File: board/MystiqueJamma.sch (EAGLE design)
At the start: 36 parts, among them IC1 7805, IC2 74LS245N, IC3 74LS245N, IC4 74LS245N, U1 AS6C4008-55PCN

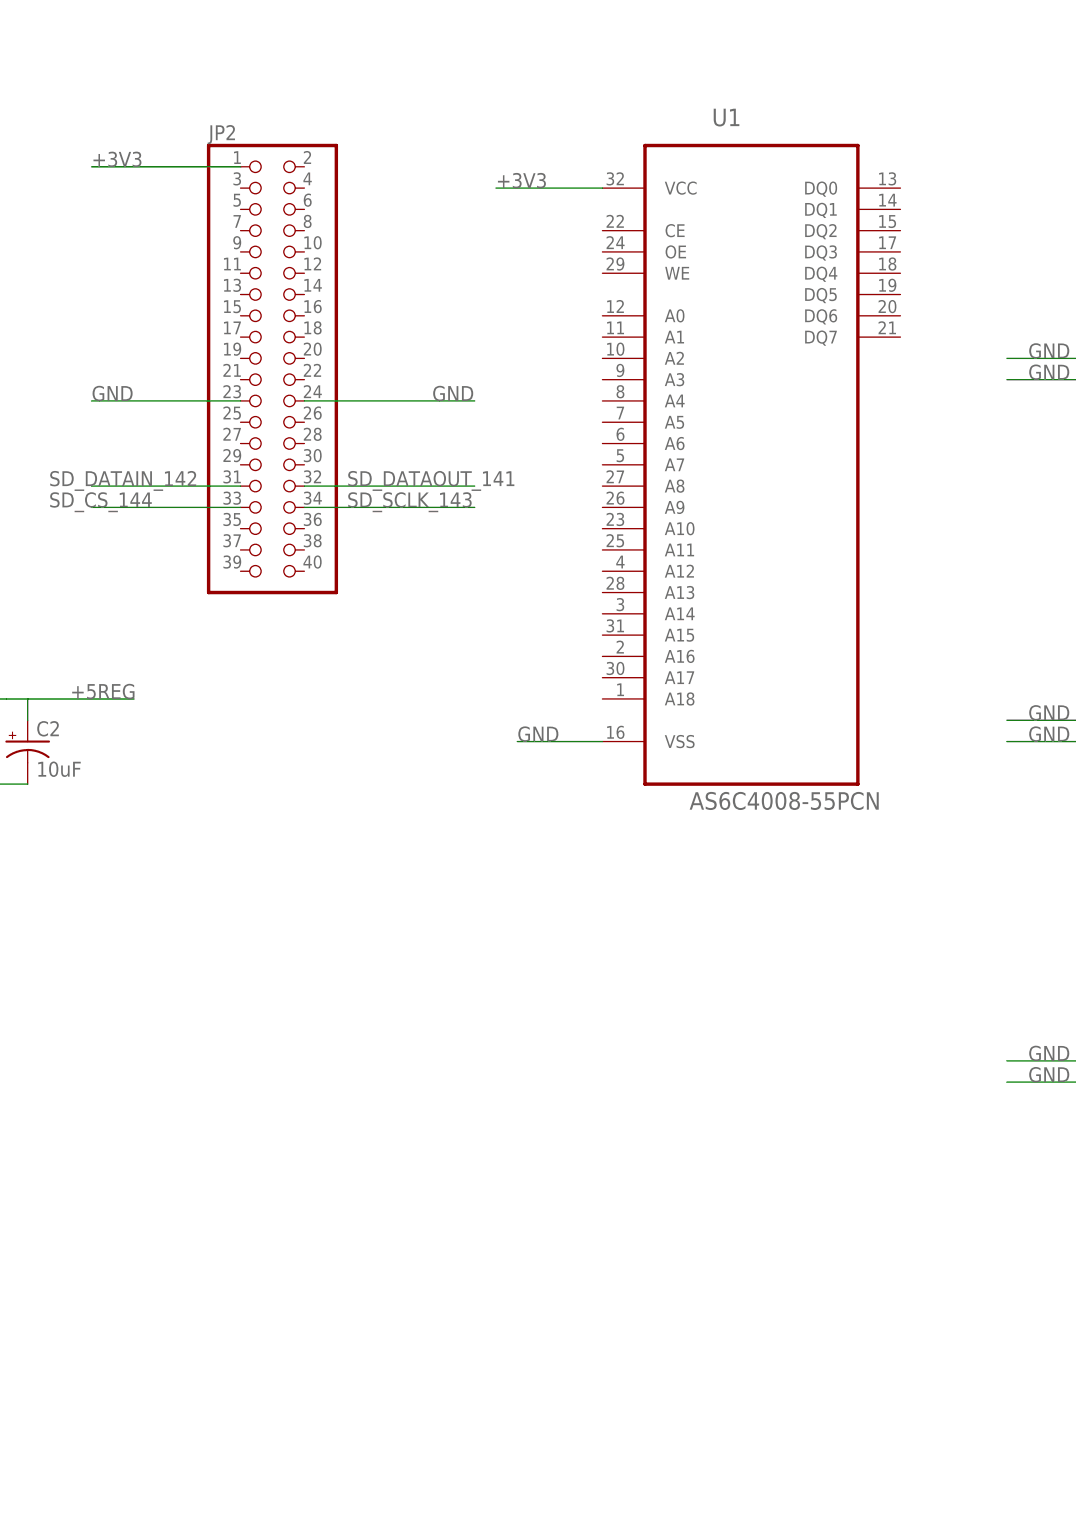
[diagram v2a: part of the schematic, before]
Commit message: changed sram ic
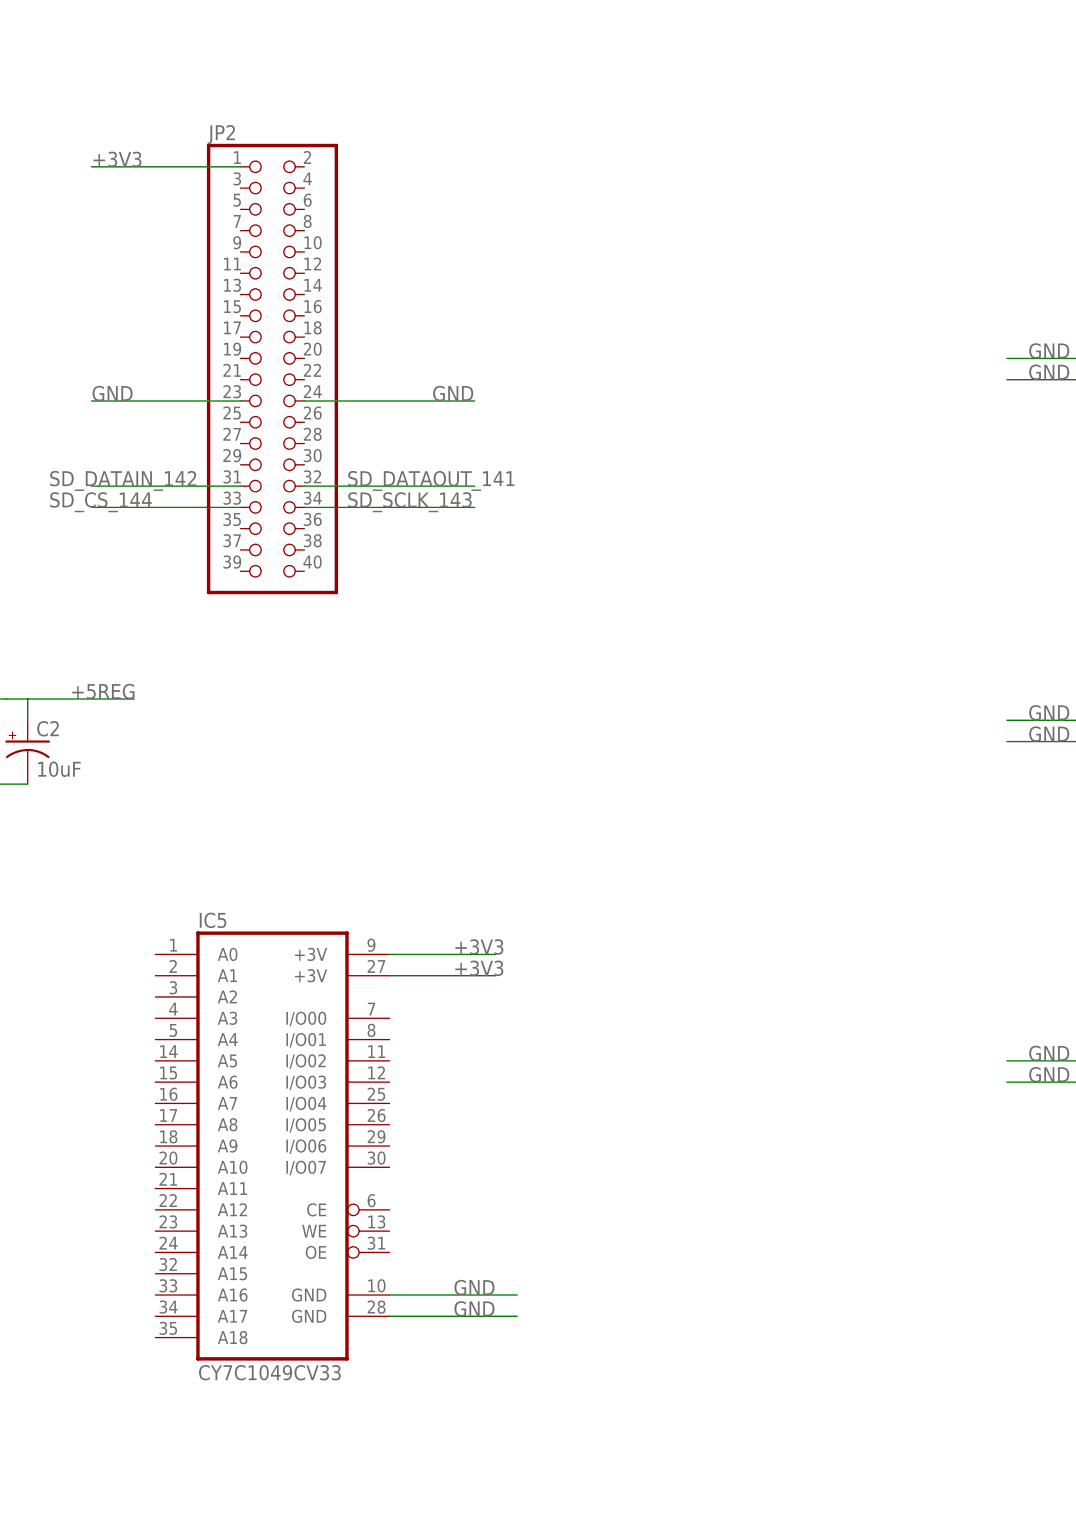
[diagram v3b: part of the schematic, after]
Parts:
- removed U1: AS6C4008-55PCN, Alliance_Memory_By_element14_Batch_1:AS6C4008-55PCN
- added IC5: CY7C1049CV33, memory-sram:CY7C1049CV33
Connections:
- net +3V3: now also IC5.+3V@1, IC5.+3V@2; no longer U1.VCC
- net GND: now also IC5.GND@1, IC5.GND@2; no longer U1.VSS
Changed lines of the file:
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@@
 <part name="C1" library="rcl-2" deviceset="CPOL-US" device="E2.5-5" value="10uF"/>
 <part name="C2" library="rcl-2" deviceset="CPOL-US" device="E2.5-5" value="10uF"/>
-<part name="U1" library="Alliance_Memory_By_element14_Batch_1" deviceset="AS6C4008-55PCN" device=""/>
 <part name="IC2" library="74xx-us" deviceset="74*245" device="N" technology="LS"/>
 <part name="R1" library="adafruit" deviceset="R-US_" device="0207/7" value="330"/>
@@
 <part name="R24" library="adafruit" deviceset="R-US_" device="0207/7" value="10k"/>
 <part name="C5" library="adafruit" deviceset="C-US" device="025-024X044" value="100nF"/>
+<part name="IC5" library="memory-sram" deviceset="CY7C1049CV33" device=""/>
 </parts>
 <sheets>
@@
 <instance part="C1" gate="G$1" x="7.62" y="12.7"/>
 <instance part="C2" gate="G$1" x="50.8" y="12.7"/>
-<instance part="U1" gate="A" x="137.16" y="48.26"/>
 <instance part="IC2" gate="A" x="190.5" y="68.58"/>
 <instance part="R1" gate="G$1" x="264.16" y="83.82"/>
@@
 <instance part="R24" gate="G$1" x="-17.78" y="-73.66" rot="R90"/>
 <instance part="C5" gate="G$1" x="-15.24" y="-96.52"/>
+<instance part="IC5" gate="G$1" x="78.74" y="-35.56"/>
 </instances>
 <busses>
@@
 </segment>
 <segment>
-<pinref part="U1" gate="A" pin="VSS"/>
-<wire x1="119.38" y1="12.7" x2="109.22" y2="12.7" width="0.1524" layer="91"/>
-<label x="109.22" y="12.7" size="1.778" layer="95"/>
-</segment>
-<segment>
 <pinref part="IC2" gate="A" pin="DIR"/>
 <wire x1="177.8" y1="58.42" x2="167.64" y2="58.42" width="0.1524" layer="91"/>
@@
 <wire x1="-15.24" y1="-101.6" x2="-15.24" y2="-106.68" width="0.1524" layer="91"/>
 <label x="-17.78" y="-109.22" size="1.778" layer="95"/>
+</segment>
+<segment>
+<pinref part="IC5" gate="G$1" pin="GND@1"/>
+<wire x1="93.98" y1="-53.34" x2="109.22" y2="-53.34" width="0.1524" layer="91"/>
+<label x="101.6" y="-53.34" size="1.778" layer="95"/>
+</segment>
+<segment>
+<pinref part="IC5" gate="G$1" pin="GND@2"/>
+<wire x1="93.98" y1="-55.88" x2="109.22" y2="-55.88" width="0.1524" layer="91"/>
+<label x="101.6" y="-55.88" size="1.778" layer="95"/>
 </segment>
 </net>
@@
 <net name="+3V3" class="0">
 <segment>
-<pinref part="U1" gate="A" pin="VCC"/>
-<wire x1="119.38" y1="78.74" x2="106.68" y2="78.74" width="0.1524" layer="91"/>
-<label x="106.68" y="78.74" size="1.778" layer="95"/>
-</segment>
-<segment>
 <pinref part="R2" gate="G$1" pin="2"/>
 <wire x1="256.54" y1="93.98" x2="256.54" y2="96.52" width="0.1524" layer="91"/>
@@
 <label x="58.42" y="81.28" size="1.778" layer="95"/>
 </segment>
-</net>
+<segment>
+<pinref part="IC5" gate="G$1" pin="+3V@1"/>
+<wire x1="93.98" y1="-12.7" x2="106.68" y2="-12.7" width="0.1524" layer="91"/>
+</segment>
+<segment>
+<pinref part="IC5" gate="G$1" pin="+3V@2"/>
+<wire x1="93.98" y1="-15.24" x2="106.68" y2="-15.24" width="0.1524" layer="91"/>
+<label x="101.6" y="-12.7" size="1.778" layer="95"/>
+<label x="101.6" y="-15.24" size="1.778" layer="95"/>
+</segment>
+</net>
